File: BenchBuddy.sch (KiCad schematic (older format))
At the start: 0 parts

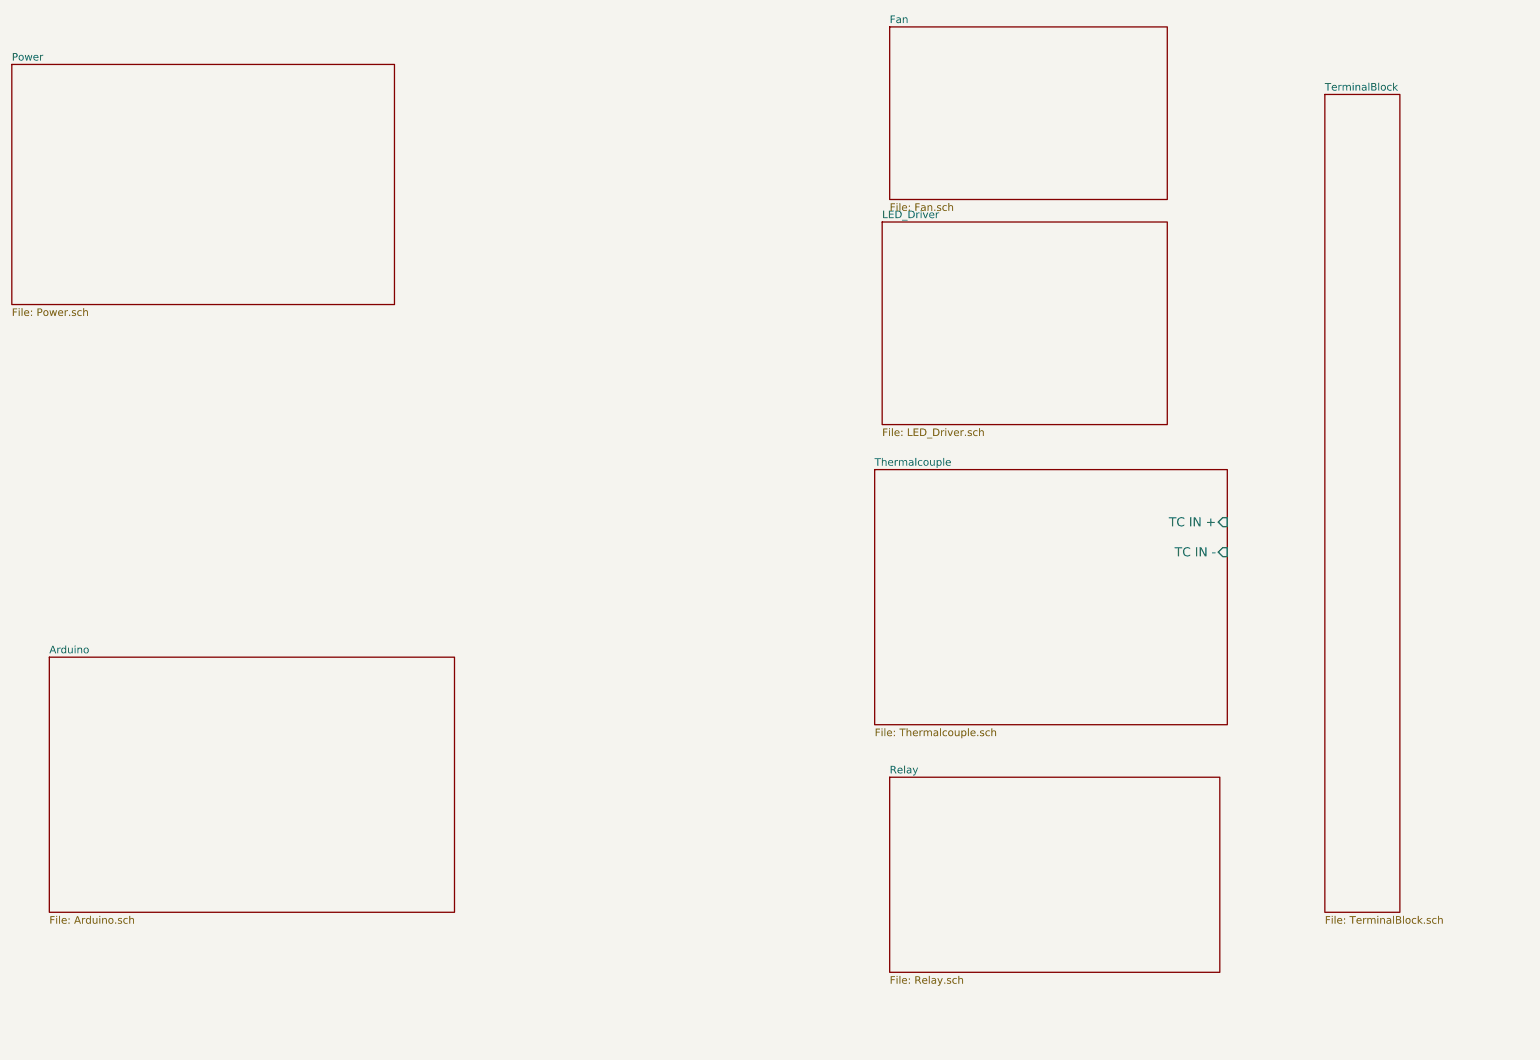
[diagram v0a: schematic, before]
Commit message: Definging inputs and outputs
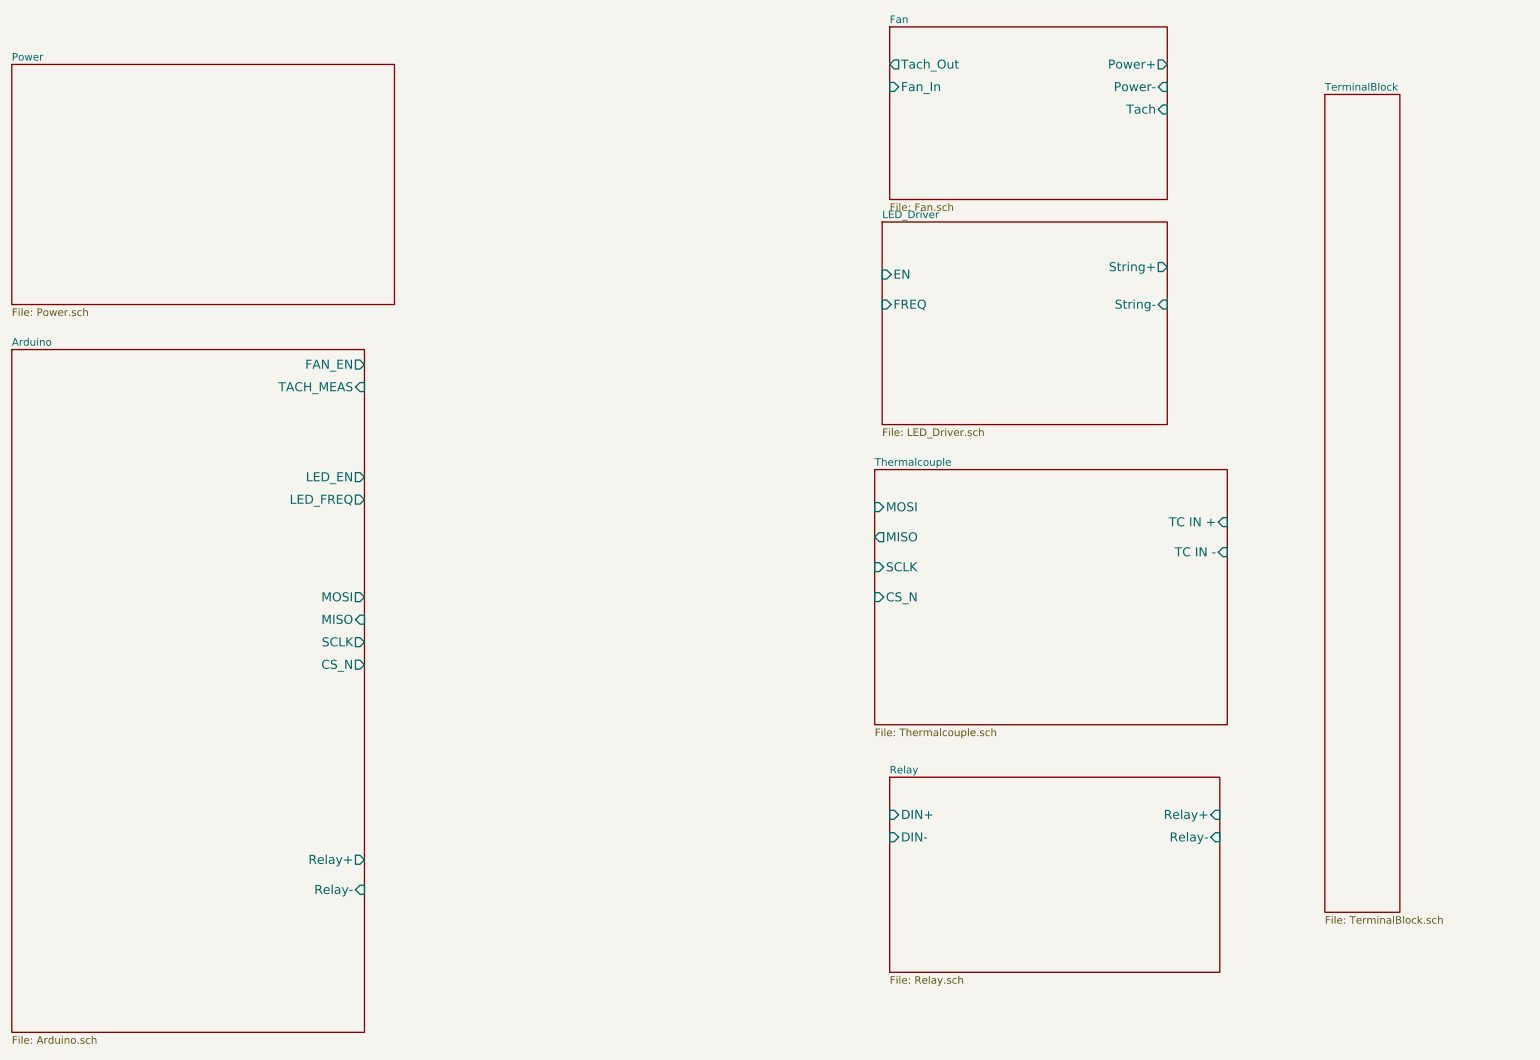
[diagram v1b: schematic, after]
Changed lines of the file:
@@
 LIBS:contrib
 LIBS:valves
+LIBS:BenchBuddy-cache
 EELAYER 27 0
 EELAYER END
@@
 Sheet 1 8
 Title ""
-Date "2 feb 2014"
+Date "3 feb 2014"
 Rev ""
 Comp ""
@@
 $EndDescr
 $Sheet
-S 1500 4850 2700 1700
+S 1250 2800 2350 4550
 U 52EEB005
 F0 "Arduino" 50
 F1 "Arduino.sch" 50
-$EndSheet
-$Sheet
-S 7000 3600 2350 1700
-U 52EEB050
-F0 "Thermalcouple" 50
-F1 "Thermalcouple.sch" 50
-F2 "TC IN +" I R 9350 3950 60
-F3 "TC IN -" I R 9350 4150 60
+F2 "Relay+" O R 3600 6200 60
+F3 "Relay-" I R 3600 6400 60
+F4 "MOSI" O R 3600 4450 60
+F5 "MISO" I R 3600 4600 60
+F6 "SCLK" O R 3600 4750 60
+F7 "CS_N" O R 3600 4900 60
+F8 "LED_EN" O R 3600 3650 60
+F9 "LED_FREQ" O R 3600 3800 60
+F10 "FAN_EN" O R 3600 2900 60
+F11 "TACH_MEAS" I R 3600 3050 60
 $EndSheet
 $Sheet
@@
 F0 "Relay" 50
 F1 "Relay.sch" 50
+F2 "DIN+" I L 7100 5900 60
+F3 "DIN-" I L 7100 6050 60
+F4 "Relay+" I R 9300 5900 60
+F5 "Relay-" I R 9300 6050 60
 $EndSheet
 $Sheet
@@
 F0 "LED_Driver" 50
 F1 "LED_Driver.sch" 50
+F2 "EN" I L 7050 2300 60
+F3 "FREQ" I L 7050 2500 60
+F4 "String+" O R 8950 2250 60
+F5 "String-" I R 8950 2500 60
 $EndSheet
 $Sheet
@@
 F0 "Fan" 50
 F1 "Fan.sch" 50
+F2 "Power+" O R 8950 900 60
+F3 "Power-" I R 8950 1050 60
+F4 "Tach" I R 8950 1200 60
+F5 "Tach_Out" O L 7100 900 60
+F6 "Fan_In" I L 7100 1050 60
 $EndSheet
 $Sheet
@@
 F1 "TerminalBlock.sch" 50
 $EndSheet
+$Sheet
+S 7000 3600 2350 1700
+U 52EEB050
+F0 "Thermalcouple" 50
+F1 "Thermalcouple.sch" 50
+F2 "TC IN +" I R 9350 3950 60
+F3 "TC IN -" I R 9350 4150 60
+F4 "MOSI" I L 7000 3850 60
+F5 "MISO" O L 7000 4050 60
+F6 "SCLK" I L 7000 4250 60
+F7 "CS_N" I L 7000 4450 60
+$EndSheet
 $EndSCHEMATC

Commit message: fan/currentdriver after chris video
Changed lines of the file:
@@
 Sheet 1 8
 Title ""
-Date "4 feb 2014"
+Date "6 feb 2014"
 Rev ""
 Comp ""
@@
 F3 "Power-" I R 8950 1050 60
 F4 "Tach" I R 8950 1200 60
-F5 "Tach_Out" O L 7100 900 60
-F6 "Fan_In" I L 7100 1050 60
+F5 "Tach_Out" O L 7100 1650 60
+F6 "Fan_In" I L 7100 800 60
+F7 "Current Measure" O L 7100 1550 60
+F8 "MOSI" I L 7100 1000 60
+F9 "MISO" O L 7100 1100 60
+F10 "CS_N" I L 7100 1200 60
+F11 "SCLK" I L 7100 1300 60
 $EndSheet
 $Sheet

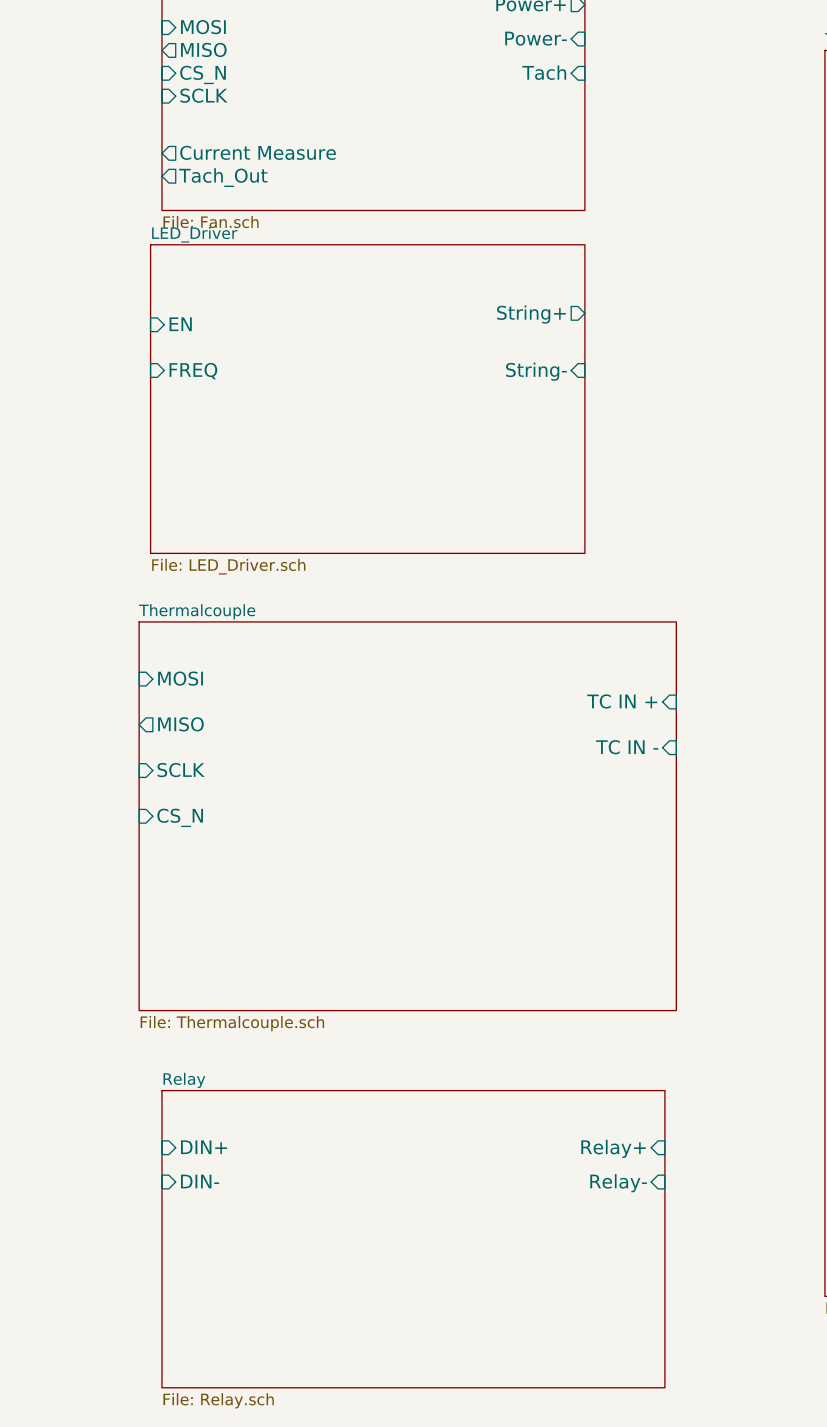
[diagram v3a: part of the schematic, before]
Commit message: Relay circuit
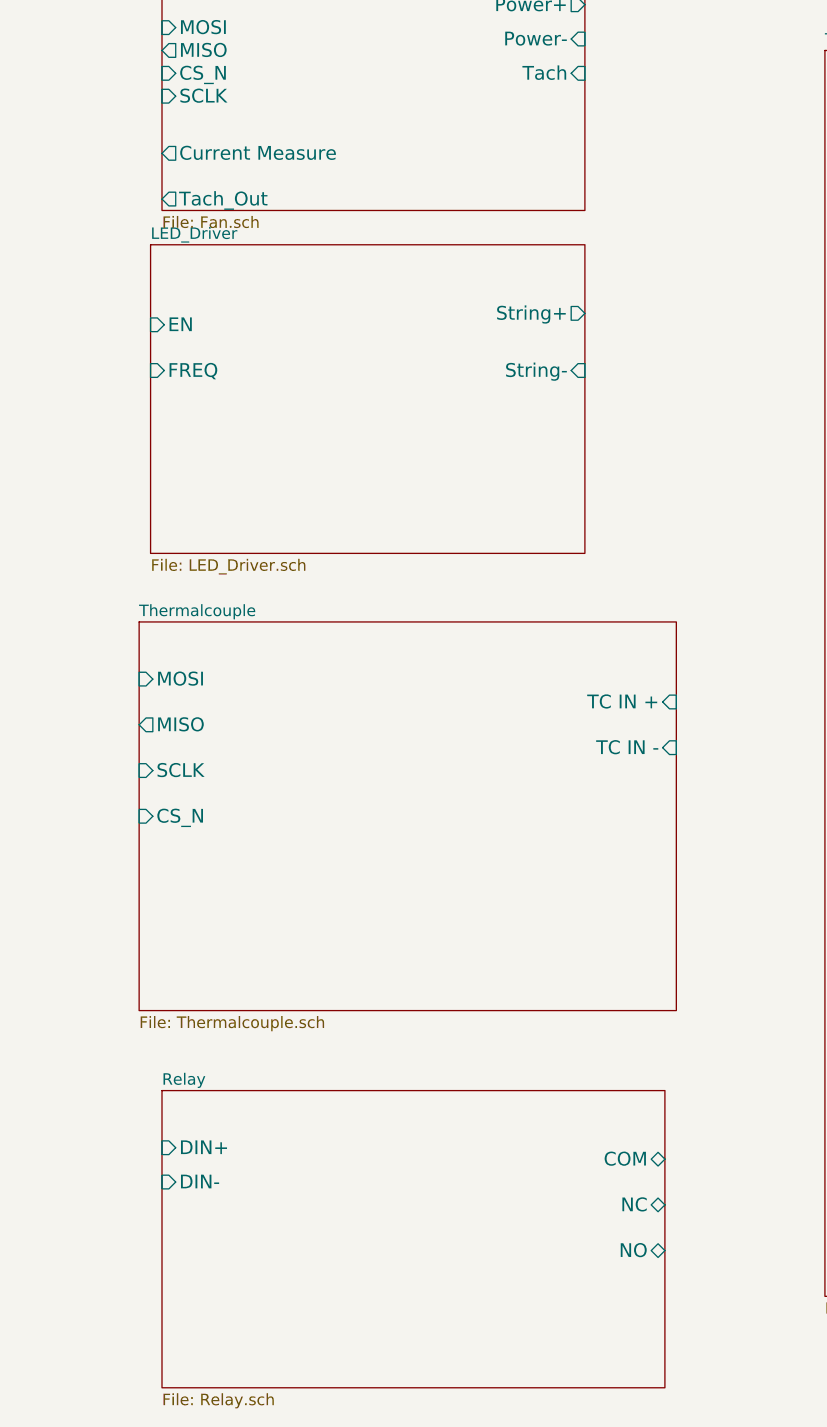
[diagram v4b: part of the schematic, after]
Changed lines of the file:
@@
 LIBS:contrib
 LIBS:valves
+LIBS:relay_spdt
 LIBS:BenchBuddy-cache
 EELAYER 27 0
@@
 F2 "DIN+" I L 7100 5900 60
 F3 "DIN-" I L 7100 6050 60
-F4 "Relay+" I R 9300 5900 60
-F5 "Relay-" I R 9300 6050 60
+F4 "NC" B R 9300 6150 60
+F5 "NO" B R 9300 6350 60
+F6 "COM" B R 9300 5950 60
 $EndSheet
 $Sheet
@@
 F3 "Power-" I R 8950 1050 60
 F4 "Tach" I R 8950 1200 60
-F5 "Tach_Out" O L 7100 1650 60
+F5 "Tach_Out" O L 7100 1750 60
 F6 "Fan_In" I L 7100 800 60
 F7 "Current Measure" O L 7100 1550 60

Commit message: Power circuit
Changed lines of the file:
@@
 $Descr A4 11693 8268
 encoding utf-8
-Sheet 1 8
+Sheet 1 9
 Title ""
 Date "6 feb 2014"
@@
 F7 "CS_N" I L 7000 4450 60
 $EndSheet
+$Sheet
+S 4200 900  2150 1600
+U 52F3A754
+F0 "PowerAdjustmentMonitor" 50
+F1 "PowerAdjustmentMonitor.sch" 50
+$EndSheet
 $EndSCHEMATC

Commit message: after power adjustment video
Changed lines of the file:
@@
 $EndDescr
 $Sheet
-S 1250 2800 2350 4550
+S 1250 2800 2050 4400
 U 52EEB005
 F0 "Arduino" 50
 F1 "Arduino.sch" 50
-F2 "Relay+" O R 3600 6200 60
-F3 "Relay-" I R 3600 6400 60
-F4 "MOSI" O R 3600 4450 60
-F5 "MISO" I R 3600 4600 60
-F6 "SCLK" O R 3600 4750 60
-F7 "CS_N" O R 3600 4900 60
-F8 "LED_EN" O R 3600 3650 60
-F9 "LED_FREQ" O R 3600 3800 60
-F10 "FAN_EN" O R 3600 2900 60
-F11 "TACH_MEAS" I R 3600 3050 60
+F2 "Relay+" O R 3300 6200 60
+F3 "Relay-" I R 3300 6400 60
+F4 "MOSI" O R 3300 4450 60
+F5 "MISO" I R 3300 4600 60
+F6 "SCLK" O R 3300 4750 60
+F7 "CS_N" O R 3300 4900 60
+F8 "LED_EN" O R 3300 3650 60
+F9 "LED_FREQ" O R 3300 3800 60
+F10 "FAN_EN" O R 3300 2900 60
+F11 "TACH_MEAS" I R 3300 3050 60
 $EndSheet
 $Sheet
-S 7100 5650 2200 1300
+S 7100 6050 1850 900
 U 52EEB072
 F0 "Relay" 50
 F1 "Relay.sch" 50
-F2 "DIN+" I L 7100 5900 60
-F3 "DIN-" I L 7100 6050 60
-F4 "NC" B R 9300 6150 60
-F5 "NO" B R 9300 6350 60
-F6 "COM" B R 9300 5950 60
+F2 "DIN+" I L 7100 6300 60
+F3 "DIN-" I L 7100 6450 60
+F4 "NC" B R 8950 6550 60
+F5 "NO" B R 8950 6750 60
+F6 "COM" B R 8950 6350 60
 $EndSheet
 $Sheet
-S 1250 900  2550 1600
+S 1250 900  2050 1200
 U 52EEB085
 F0 "Power" 50
@@
 $EndSheet
 $Sheet
-S 7050 1950 1900 1350
+S 7100 3550 1850 850
 U 52EEB0B1
 F0 "LED_Driver" 50
 F1 "LED_Driver.sch" 50
-F2 "EN" I L 7050 2300 60
-F3 "FREQ" I L 7050 2500 60
-F4 "String+" O R 8950 2250 60
-F5 "String-" I R 8950 2500 60
+F2 "EN" I L 7100 3900 60
+F3 "FREQ" I L 7100 4100 60
+F4 "String+" O R 8950 3850 60
+F5 "String-" I R 8950 4100 60
 $EndSheet
 $Sheet
-S 7100 650  1850 1150
+S 7100 2100 1850 1150
 U 52EEB0CE
 F0 "Fan" 50
 F1 "Fan.sch" 50
-F2 "Power+" O R 8950 900 60
-F3 "Power-" I R 8950 1050 60
-F4 "Tach" I R 8950 1200 60
-F5 "Tach_Out" O L 7100 1750 60
-F6 "Fan_In" I L 7100 800 60
-F7 "Current Measure" O L 7100 1550 60
-F8 "MOSI" I L 7100 1000 60
-F9 "MISO" O L 7100 1100 60
-F10 "CS_N" I L 7100 1200 60
-F11 "SCLK" I L 7100 1300 60
+F2 "Power+" O R 8950 2350 60
+F3 "Power-" I R 8950 2500 60
+F4 "Tach" I R 8950 2650 60
+F5 "Tach_Out" O L 7100 3200 60
+F6 "Fan_In" I L 7100 2250 60
+F7 "Current Measure" O L 7100 3000 60
+F8 "MOSI" I L 7100 2450 60
+F9 "MISO" O L 7100 2550 60
+F10 "CS_N" I L 7100 2650 60
+F11 "SCLK" I L 7100 2750 60
 $EndSheet
 $Sheet
-S 10000 1100 500  5450
+S 10250 800  500  5450
 U 52EEB0FB
 F0 "TerminalBlock" 50
@@
 $EndSheet
 $Sheet
-S 7000 3600 2350 1700
+S 7100 4750 1850 1050
 U 52EEB050
 F0 "Thermalcouple" 50
 F1 "Thermalcouple.sch" 50
-F2 "TC IN +" I R 9350 3950 60
-F3 "TC IN -" I R 9350 4150 60
-F4 "MOSI" I L 7000 3850 60
-F5 "MISO" O L 7000 4050 60
-F6 "SCLK" I L 7000 4250 60
-F7 "CS_N" I L 7000 4450 60
+F2 "TC IN +" I R 8950 5100 60
+F3 "TC IN -" I R 8950 5300 60
+F4 "MOSI" I L 7100 5000 60
+F5 "MISO" O L 7100 5200 60
+F6 "SCLK" I L 7100 5400 60
+F7 "CS_N" I L 7100 5600 60
 $EndSheet
 $Sheet
@@
 F0 "PowerAdjustmentMonitor" 50
 F1 "PowerAdjustmentMonitor.sch" 50
+F2 "V+_ADJ" O R 6350 1150 60
+F3 "V-_ADJ" O R 6350 1300 60
+F4 "3V3_MON" O L 4200 1450 60
+F5 "5V_MON" O L 4200 1600 60
+F6 "V+_ADJ_MON" O L 4200 1800 60
+F7 "V-_ADJ_MON" O L 4200 1950 60
+F8 "V+_CURR_MON" O L 4200 2400 60
+F9 "V-_CURR_MON" O L 4200 2150 60
 $EndSheet
 $EndSCHEMATC

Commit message: After led drier module
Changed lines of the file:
@@
 LIBS:valves
 LIBS:relay_spdt
+LIBS:BenchBuddy
 LIBS:BenchBuddy-cache
 EELAYER 27 0
@@
 F0 "LED_Driver" 50
 F1 "LED_Driver.sch" 50
-F2 "EN" I L 7100 3900 60
-F3 "FREQ" I L 7100 4100 60
-F4 "String+" O R 8950 3850 60
-F5 "String-" I R 8950 4100 60
+F2 "String+" O R 8950 3850 60
+F3 "String-" I R 8950 4100 60
+F4 "LED_EN_PWM" I L 7100 3900 60
 $EndSheet
 $Sheet
